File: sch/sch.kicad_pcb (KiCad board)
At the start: 2 copper layers, 99.1 x 49.5 mm, 61 parts, among them P1 CONN_01X02, P12 CONN_01X03, P13 CONN_01X03, P2 CONN_02X05, P4 CONN_01X06, P5 BNC, P6 Digital, P7 Analog, U1 PT4115, U10 DS18B20, U11 DS18B20, U2 PT4115, U3 PT4115, U4 PT4115, U5 PT4115, U6 PT4115, U7 LM324, U9 LM7805CT

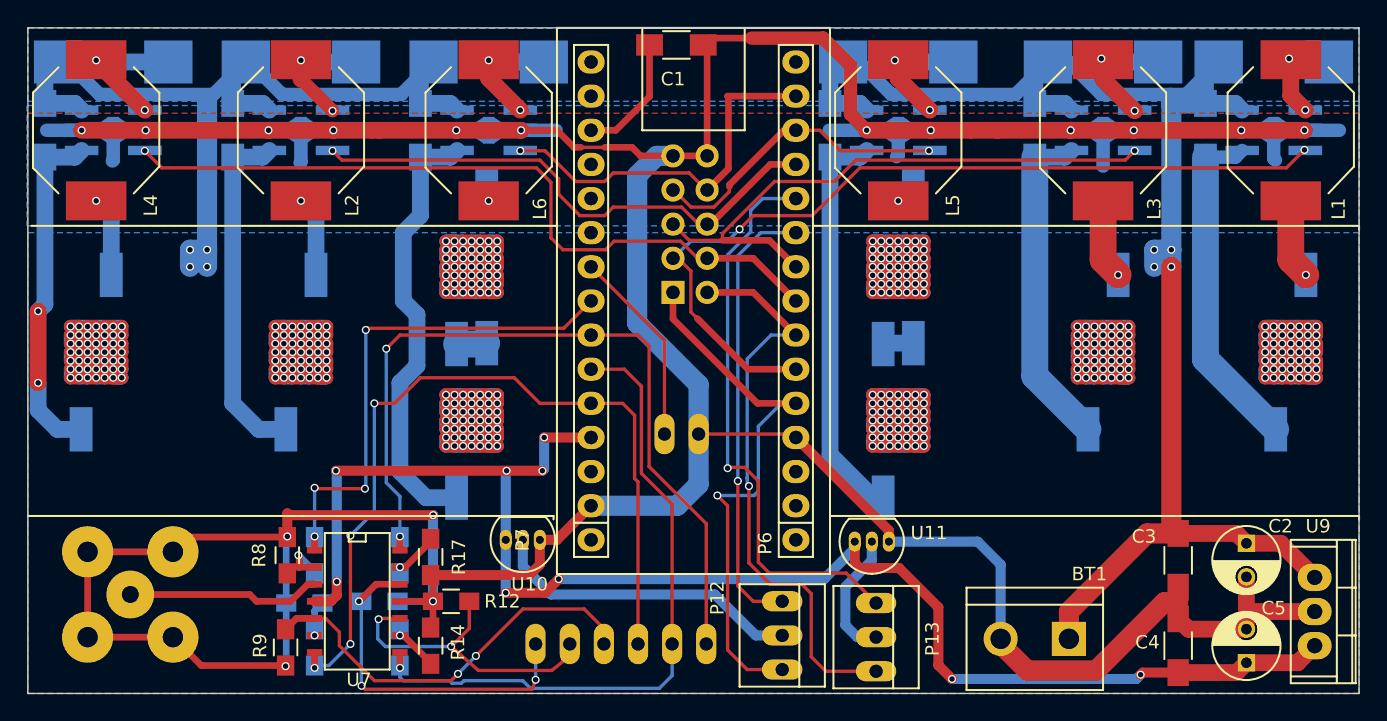
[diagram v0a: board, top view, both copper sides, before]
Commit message: Fixed minor details in pcb and added openings in solder mas for thermal vias behind led
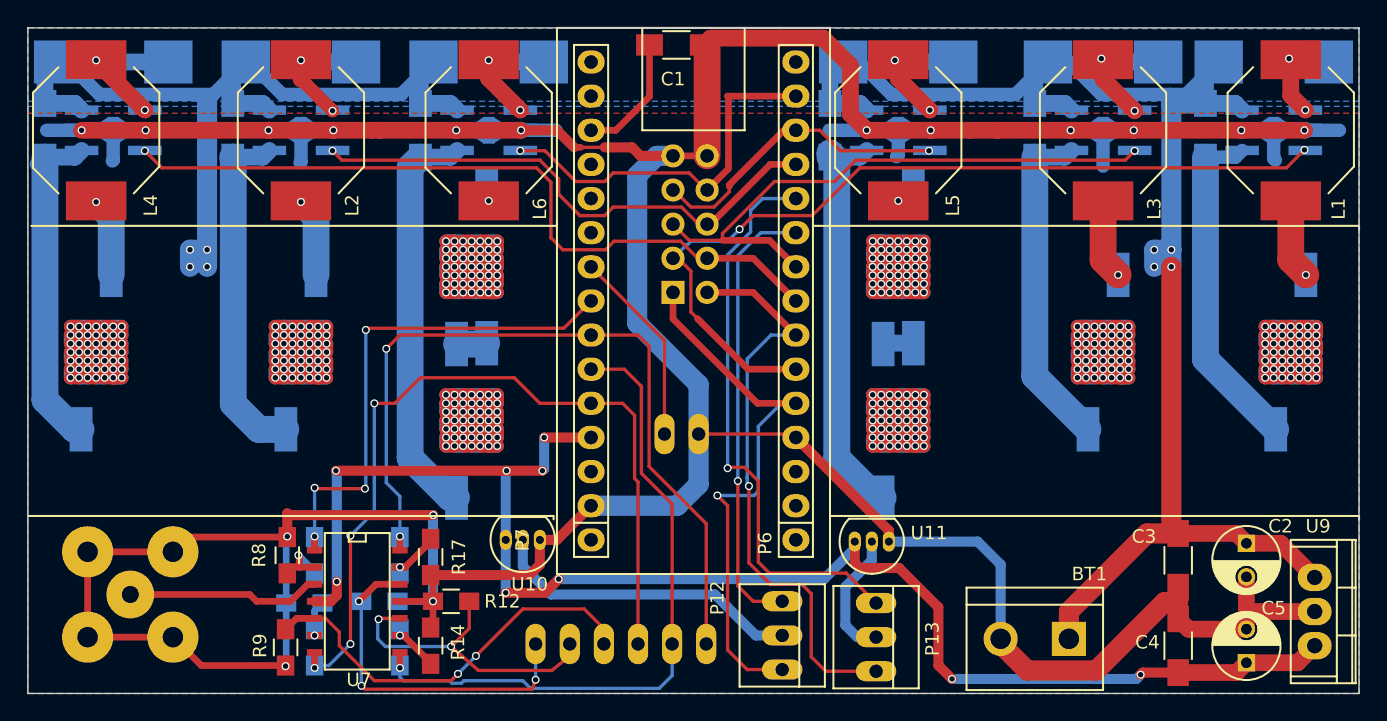
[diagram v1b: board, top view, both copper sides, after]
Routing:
- net Net-(D12-PadANOD): track 32.8 -> 30.3 mm
- net Net-(D11-PadANOD): track 30.4 -> 31.6 mm
- net Net-(D4-PadANOD): track 25.8 -> 25.3 mm, vias 2 -> 0
